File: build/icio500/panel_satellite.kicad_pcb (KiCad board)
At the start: 2 copper layers, 38.1 x 133.3 mm, 30 parts, among them J1 Conn_02x10_Odd_Even, U1 IS31FL3236

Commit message: Fix 3D offsets finally (Offset AFTER rotation) and autoroute main board U6 connections
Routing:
- net LED_3: track 0.00 -> 45.1 mm
- net LED_9: track 0.00 -> 34.3 mm
- net LED_8: track 0.00 -> 25.9 mm
- net GND: track 0.00 -> 20.9 mm
- net SDA: track 0.00 -> 20.1 mm
- net SCL: track 0.00 -> 15.0 mm
- net LED_7: track 0.00 -> 13.3 mm
- net LED_7_MID: track 0.00 -> 9.06 mm
- net LED_6_MID: track 0.00 -> 9.06 mm
- net LED_8_MID: track 0.00 -> 8.46 mm
- net LED_9_MID: track 0.00 -> 8.26 mm
- net LED_10_MID: track 0.00 -> 8.26 mm
- net 0: vias 0 -> 6

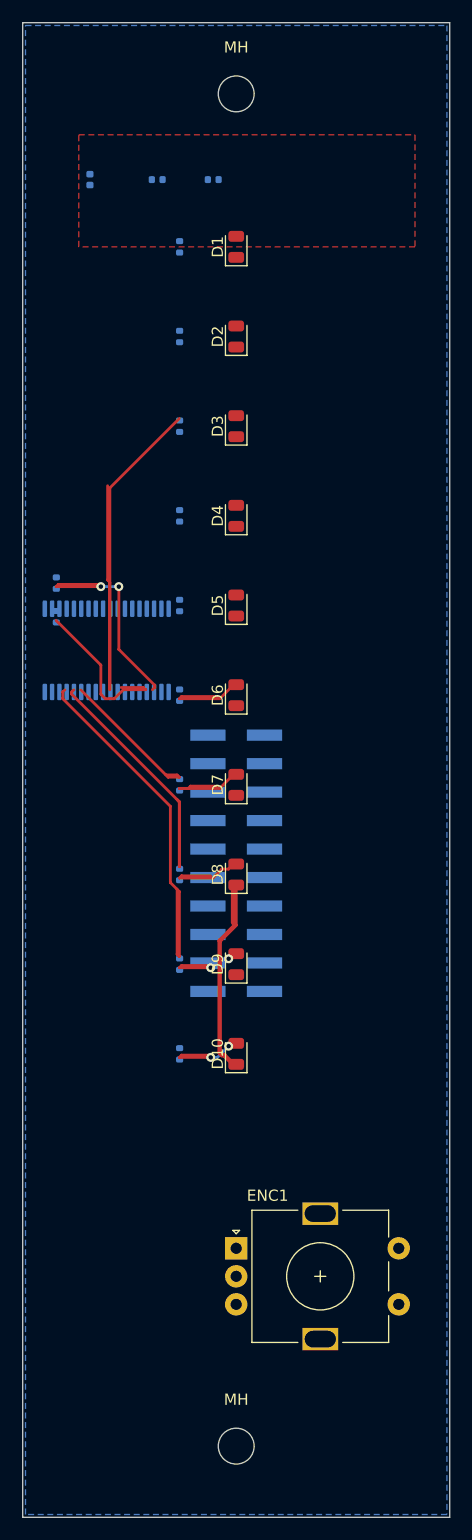
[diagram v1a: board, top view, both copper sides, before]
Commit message: Restore VPR summer board outline (Y=160mm, 26mm bottom notch), align lower bracket BR2, purge vestigial files
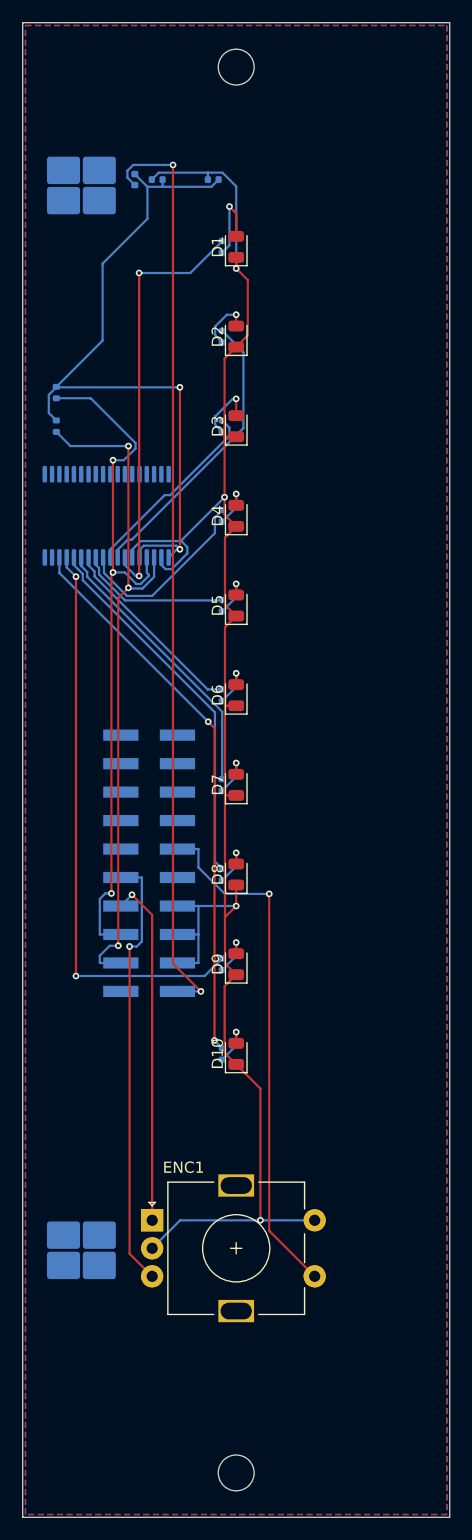
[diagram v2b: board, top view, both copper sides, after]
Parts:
- added BR1: WP-SMRA-M3, Mounting_Wuerth_WP-SMRA-M3_L7mm_7466303_Horizontal, B.Cu at (105.2, 114.5)
- added BR2: WP-SMRA-M3, Mounting_Wuerth_WP-SMRA-M3_L7mm_7466303_Horizontal, B.Cu at (105.2, 209.5)
- moved R12 20.0 mm to (103.0, 133.0)
- moved R11 14.0 mm to (103.0, 136.0)
- moved U1 12.0 mm to (107.5, 144.0)
- moved ENC1 7.91 mm to (111.5, 206.8)
- moved J1 7.77 mm to (111.3, 175.0)
- moved FB1 4.00 mm to (110.0, 114.0)
- moved R1 3.80 mm to (117.8, 120.0)
- moved R10 3.80 mm to (117.8, 192.0)
- moved R2 3.80 mm to (117.8, 128.0)
- moved R3 3.80 mm to (117.8, 136.0)
- moved R4 3.80 mm to (117.8, 144.0)
- moved R5 3.80 mm to (117.8, 152.0)
- moved R6 3.80 mm to (117.8, 160.0)
- moved R7 3.80 mm to (117.8, 168.0)
- moved R8 3.80 mm to (117.8, 176.0)
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- renumbered MH to MH1, MH to MH2
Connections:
- C1 pad 1: (no net) -> +3V3
- C1 pad 2: (no net) -> GND
- C2 pad 1: (no net) -> +3V3
- C2 pad 2: (no net) -> GND
- D1 pad 1: (no net) -> GND
- D1 pad 2: (no net) -> LED_1_MID
- D2 pad 1: (no net) -> GND
- D2 pad 2: (no net) -> LED_2_MID
- D3 pad 1: (no net) -> GND
- D3 pad 2: (no net) -> LED_3_MID
- D4 pad 1: (no net) -> GND
- D4 pad 2: (no net) -> LED_4_MID
- D5 pad 1: (no net) -> GND
- D5 pad 2: (no net) -> LED_5_MID
- D6 pad 1: (no net) -> GND
- D7 pad 1: (no net) -> GND
- D9 pad 1: (no net) -> GND
- ENC1 pad A: (no net) -> ENC_A
- ENC1 pad B: (no net) -> ENC_B
- ENC1 pad C: (no net) -> GND
- ENC1 pad S1: (no net) -> ENC_SW
- ENC1 pad S2: (no net) -> GND
- FB1 pad 1: (no net) -> +3V3_IN
- FB1 pad 2: (no net) -> +3V3
- J1 pad 12: (no net) -> ENC_SW
- J1 pad 2: (no net) -> +3V3_IN
- J1 pad 3: (no net) -> SDA
- J1 pad 4: (no net) -> GND
- J1 pad 5: (no net) -> SCL
- J1 pad 6: (no net) -> GND
- J1 pad 7: (no net) -> ENC_A
- J1 pad 8: (no net) -> GND
- J1 pad 9: (no net) -> ENC_B
- R1 pad 1: (no net) -> LED_1_MID
- R1 pad 2: (no net) -> LED_1
- R11 pad 2: (no net) -> +3V3
- R12 pad 2: (no net) -> +3V3
- R4 pad 1: (no net) -> LED_4_MID
- R4 pad 2: (no net) -> LED_4
- R5 pad 1: (no net) -> LED_5_MID
- R5 pad 2: (no net) -> LED_5
- R6 pad 2: (no net) -> LED_6
- U1 pad 1: (no net) -> +3V3
- U1 pad 16: (no net) -> LED_10
- U1 pad 2: (no net) -> GND
- U1 pad 5: (no net) -> +3V3
- U1 pad 6: (no net) -> GND
- U1 pad 7: (no net) -> LED_1
- U1 pad 8: (no net) -> LED_2
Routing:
- net GND: track 20.9 -> 159.2 mm, vias 0 -> 4
- net +3V3_IN: track 0.00 -> 82.7 mm, vias 0 -> 2
- net +3V3: track 0.00 -> 65.0 mm, vias 0 -> 2
- net LED_10: track 0.00 -> 49.8 mm, vias 0 -> 2
- net SCL: track 15.0 -> 62.3 mm, vias 0 -> 3
- net ENC_SW: track 0.00 -> 46.6 mm, vias 0 -> 1
- net SDA: track 20.1 -> 60.9 mm, vias 0 -> 3
- net ENC_B: track 0.00 -> 39.1 mm, vias 0 -> 1
- net LED_1: track 0.00 -> 38.0 mm, vias 0 -> 2
- net ENC_A: track 0.00 -> 31.2 mm, vias 0 -> 1
- net LED_3: track 45.1 -> 17.2 mm
- net LED_2: track 0.00 -> 25.9 mm
- net LED_6: track 0.00 -> 17.5 mm
- net LED_9: track 34.3 -> 51.4 mm, vias 0 -> 2
- net LED_4: track 0.00 -> 16.8 mm
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- added copper zone on B.Cu, net GND
- added copper zone on F.Cu, net GND
- removed copper zone on B.Cu, net (none)
- removed copper zone on F.Cu, net (none)

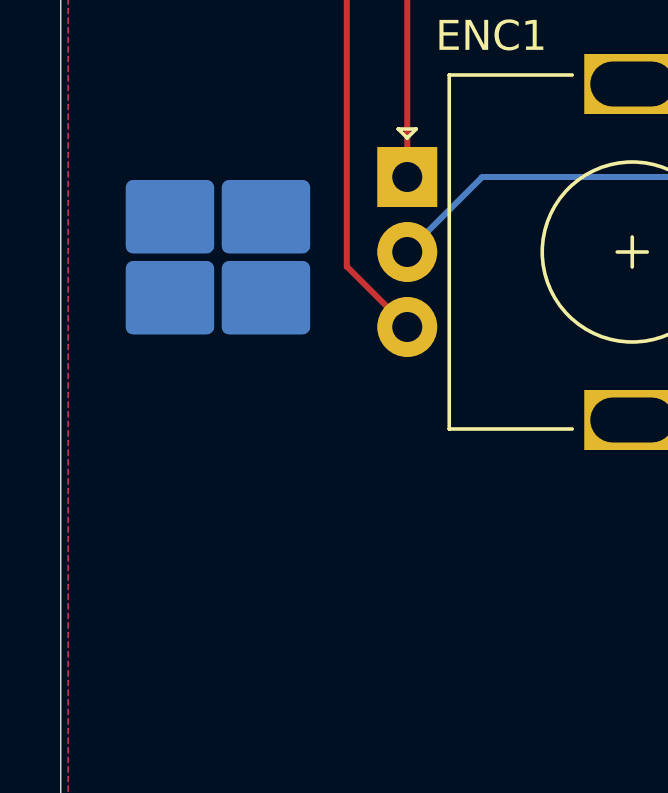
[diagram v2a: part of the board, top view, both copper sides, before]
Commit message: Finalize VPR-500 mechanical mating, zero-DRC routing, unit 3D model scale, and JLCPCB packages
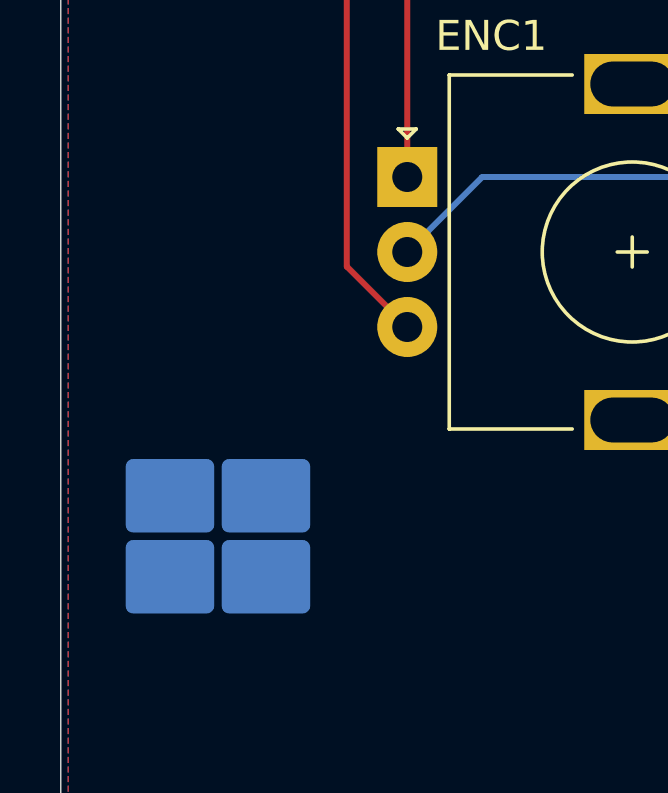
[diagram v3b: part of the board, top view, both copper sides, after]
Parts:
- moved BR2 9.30 mm to (105.2, 218.8)
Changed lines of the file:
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@@
 	(footprint "Mounting_Wuerth_WP-SMRA-M3_L7mm_7466303_Horizontal"
 		(layer "B.Cu")
-		(at 105.24 209.525)
+		(at 105.24 218.825)
 		(descr "Right-angle SMD mounting Hardware, inside threaded M3, length 7m, total height 5mm, Würth electronics 7466303 (https://www.we-online.com/components/products/datasheet/7466303.pdf)")
 		(tags "threaded screw")

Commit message: Restore authentic VPR-500 carrier board outline (Y=55-160mm, 26mm notch) and concentric 3-point mating
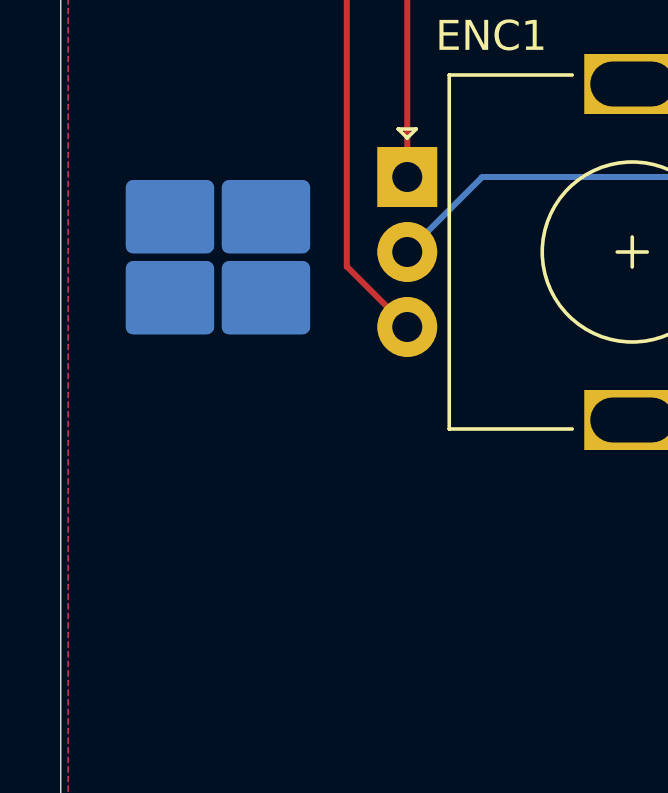
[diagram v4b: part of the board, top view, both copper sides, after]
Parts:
- moved BR2 9.30 mm to (105.2, 209.5)
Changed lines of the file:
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@@
 	(footprint "Mounting_Wuerth_WP-SMRA-M3_L7mm_7466303_Horizontal"
 		(layer "B.Cu")
-		(at 105.24 218.825)
+		(at 105.24 209.525)
 		(descr "Right-angle SMD mounting Hardware, inside threaded M3, length 7m, total height 5mm, Würth electronics 7466303 (https://www.we-online.com/components/products/datasheet/7466303.pdf)")
 		(tags "threaded screw")

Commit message: Restore finished 10-27 faceplate & satellite; maintain summer VPR card edge with zero DRC violations
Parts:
- removed BR1, BR2: WP-SMRA-M3, Mounting_Wuerth_WP-SMRA-M3_L7mm_7466303_Horizontal
- moved R12 20.0 mm to (103.0, 153.0)
- moved R11 14.0 mm to (103.0, 150.0)
- moved U1 12.0 mm to (107.5, 156.0)
- moved ENC1 7.91 mm to (119.0, 209.3)
- moved J1 7.77 mm to (119.0, 175.0)
- moved FB1 4.00 mm to (106.0, 114.0)
- moved R1 3.80 mm to (114.0, 120.0)
- moved R10 3.80 mm to (114.0, 192.0)
- moved R2 3.80 mm to (114.0, 128.0)
- moved R3 3.80 mm to (114.0, 136.0)
- moved R4 3.80 mm to (114.0, 144.0)
- moved R5 3.80 mm to (114.0, 152.0)
- moved R6 3.80 mm to (114.0, 160.0)
- moved R7 3.80 mm to (114.0, 168.0)
- moved R8 3.80 mm to (114.0, 176.0)
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- renumbered MH1 to MH, MH2 to MH
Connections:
- C1 pad 1: +3V3 -> (no net)
- C1 pad 2: GND -> (no net)
- C2 pad 1: +3V3 -> (no net)
- C2 pad 2: GND -> (no net)
- D1 pad 1: GND -> (no net)
- D1 pad 2: LED_1_MID -> (no net)
- D2 pad 1: GND -> (no net)
- D2 pad 2: LED_2_MID -> (no net)
- D3 pad 1: GND -> (no net)
- D3 pad 2: LED_3_MID -> (no net)
- D4 pad 1: GND -> (no net)
- D4 pad 2: LED_4_MID -> (no net)
- D5 pad 1: GND -> (no net)
- D5 pad 2: LED_5_MID -> (no net)
- D6 pad 1: GND -> (no net)
- D7 pad 1: GND -> (no net)
- D9 pad 1: GND -> (no net)
- ENC1 pad A: ENC_A -> (no net)
- ENC1 pad B: ENC_B -> (no net)
- ENC1 pad C: GND -> (no net)
- ENC1 pad S1: ENC_SW -> (no net)
- ENC1 pad S2: GND -> (no net)
- FB1 pad 1: +3V3_IN -> (no net)
- FB1 pad 2: +3V3 -> (no net)
- J1 pad 12: ENC_SW -> (no net)
- J1 pad 2: +3V3_IN -> (no net)
- J1 pad 3: SDA -> (no net)
- J1 pad 4: GND -> (no net)
- J1 pad 5: SCL -> (no net)
- J1 pad 6: GND -> (no net)
- J1 pad 7: ENC_A -> (no net)
- J1 pad 8: GND -> (no net)
- J1 pad 9: ENC_B -> (no net)
- R1 pad 1: LED_1_MID -> (no net)
- R1 pad 2: LED_1 -> (no net)
- R11 pad 2: +3V3 -> (no net)
- R12 pad 2: +3V3 -> (no net)
- R4 pad 1: LED_4_MID -> (no net)
- R4 pad 2: LED_4 -> (no net)
- R5 pad 1: LED_5_MID -> (no net)
- R5 pad 2: LED_5 -> (no net)
- R6 pad 2: LED_6 -> (no net)
- U1 pad 1: +3V3 -> (no net)
- U1 pad 16: LED_10 -> (no net)
- U1 pad 2: GND -> (no net)
- U1 pad 5: +3V3 -> (no net)
- U1 pad 6: GND -> (no net)
- U1 pad 7: LED_1 -> (no net)
- U1 pad 8: LED_2 -> (no net)
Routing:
- net GND: track 159.2 -> 20.9 mm, vias 4 -> 0
- net +3V3_IN: track 82.7 -> 0.00 mm, vias 2 -> 0
- net +3V3: track 65.0 -> 0.00 mm, vias 2 -> 0
- net LED_10: track 49.8 -> 0.00 mm, vias 2 -> 0
- net SCL: track 62.3 -> 15.0 mm, vias 3 -> 0
- net ENC_SW: track 46.6 -> 0.00 mm, vias 1 -> 0
- net SDA: track 60.9 -> 20.1 mm, vias 3 -> 0
- net ENC_B: track 39.1 -> 0.00 mm, vias 1 -> 0
- net LED_1: track 38.0 -> 0.00 mm, vias 2 -> 0
- net ENC_A: track 31.2 -> 0.00 mm, vias 1 -> 0
- net LED_3: track 17.2 -> 45.1 mm
- net LED_2: track 25.9 -> 0.00 mm
- net LED_6: track 17.5 -> 0.00 mm
- net LED_9: track 51.4 -> 34.3 mm, vias 2 -> 0
- net LED_4: track 16.8 -> 0.00 mm
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- added copper zone on B.Cu, net (none)
- added copper zone on F.Cu, net (none)
- removed copper zone on B.Cu, net GND
- removed copper zone on F.Cu, net GND
